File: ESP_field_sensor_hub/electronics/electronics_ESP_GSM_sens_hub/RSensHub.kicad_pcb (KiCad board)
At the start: 2 copper layers, 117 x 107 mm, 48 parts, among them J1 RJ45_Shielded, J2 RJ45_Shielded, J3 Conn_01x12_Male, J4 Conn_01x04_Female, Q4 IRF540N, U1 MAX48_module, U10 PC817, U11 PC817, U12 PC817, U2 5V5ADCDC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

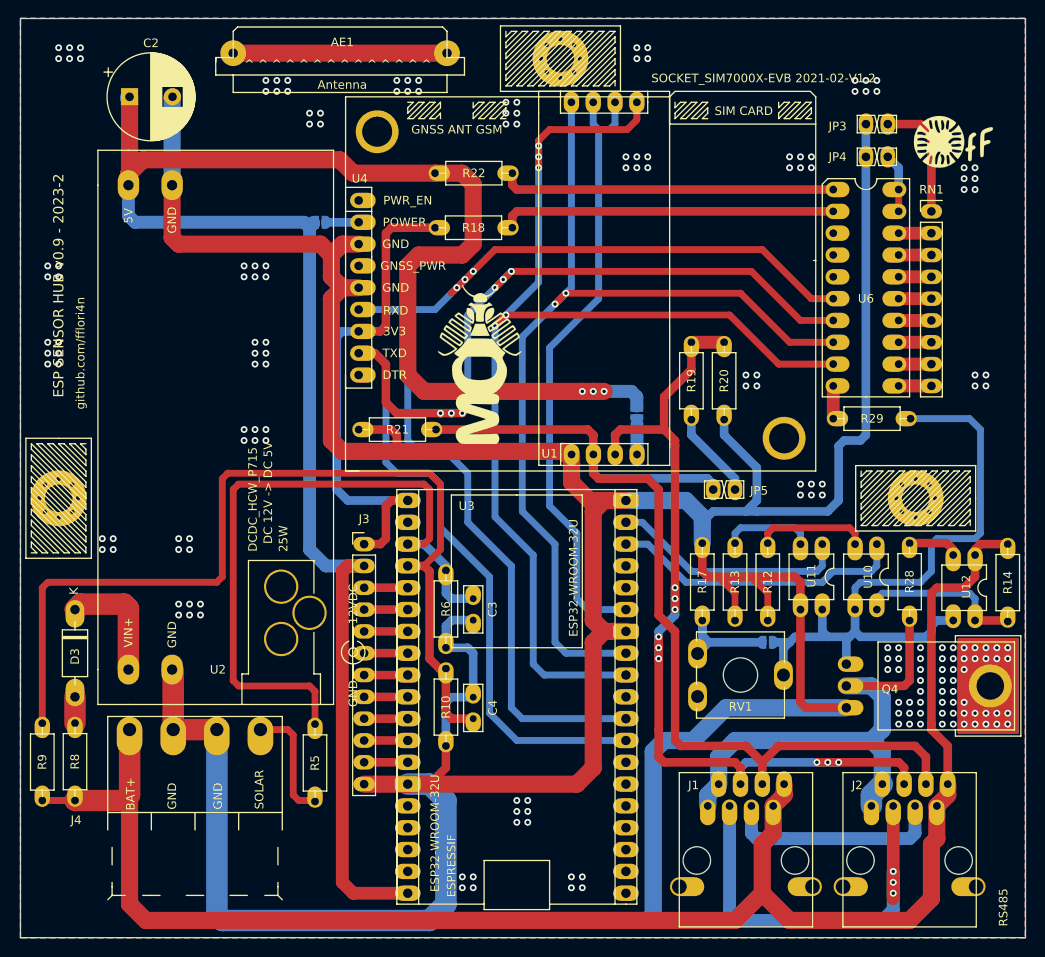
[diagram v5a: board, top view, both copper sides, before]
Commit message: started working on GNSS time and NTP functionality, ESP32 timekeeping works, just need to update it from modem. need to parse the GNSS status for string. Played around with chatGPT, and got a fairly good solution for converting datetimeString to unix time. @TODO: the SIM7000 class makes little sense, needs a refactoring. I have functions for geting CSQ and GNSS data from modem in a totally different class.
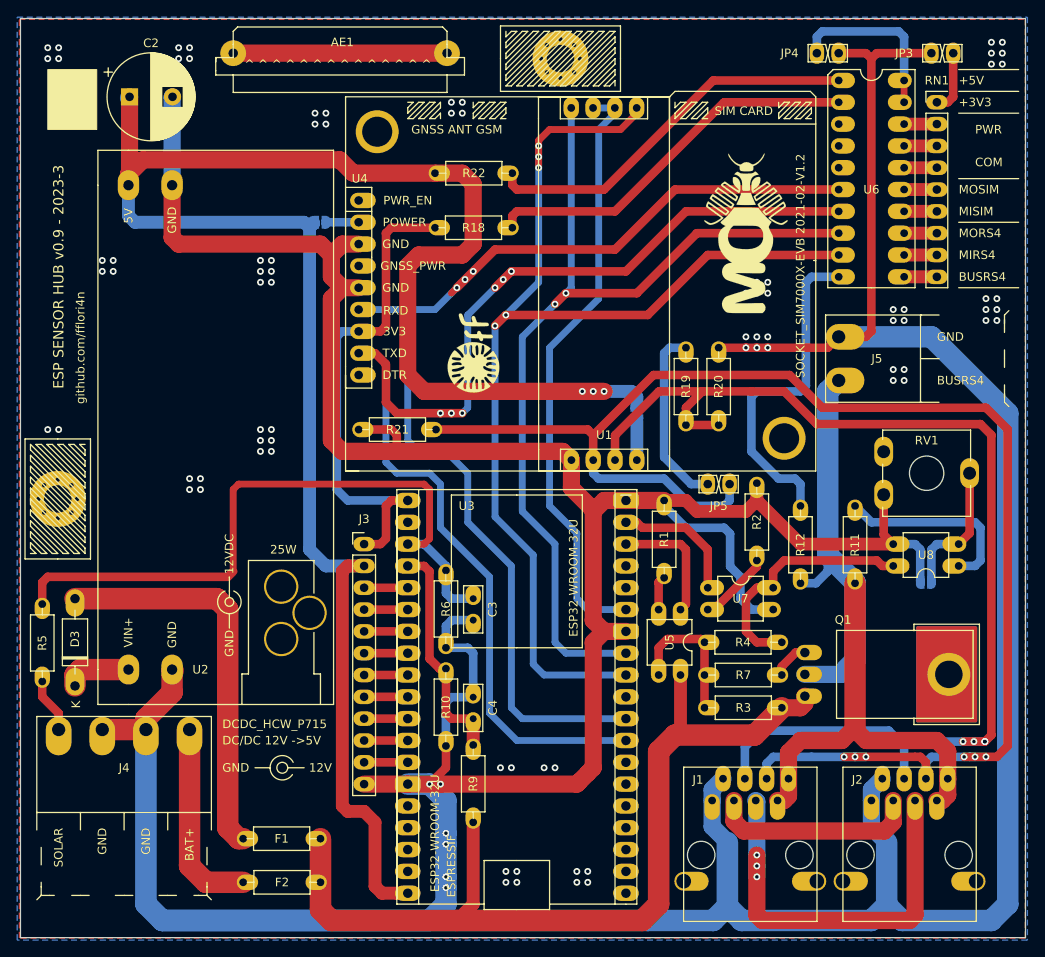
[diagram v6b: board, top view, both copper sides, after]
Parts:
- removed the G*** at (353.8, 62.2)
- removed the G*** at (358.4, 115.8)
- removed the G*** at (408.9, 36.3)
- removed Q4: IRF540N, myComponents:TO-220-3_Horizontal_TabDown_bothSides
- removed R13: 330R, myComponents:resistor0.25,9mm
- removed R14, R28, R29: 1K, myComponents:resistor0.25,9mm
- removed R17: 100K, myComponents:resistor0.25,9mm
- removed the REF** at (304.8, 77.9)
- removed the REF** at (404.6, 77.9)
- removed U10, U11, U12: PC817, myComponents:optoCouplerDIP4
- added F2: 0R, myComponents:resistor0.25,9mm, F.Cu at (335.3, 122.6)
- added G***: LOGO, myComponents:ma_Logo, B.Cu at (382.3, 38.7)
- added G***: LOGO, myComponents:xffLogo, B.Cu at (361.9, 115.6)
- added G***: LOGO, myComponents:xffLogo, F.Cu at (353.1, 61.0)
- added G***: LOGO, myComponents:ma_Logo, F.Cu at (384.8, 47.0)
- added J5: Conn_01x02_Male, myComponents:TerminalBlockRemovablex2, F.Cu at (395.6, 64.1)
- added Q1: IRF9540, myComponents:TO-220-3_Horizontal_TabDown_bothSides, F.Cu at (391.7, 95.8)
- added R1: 330R, myComponents:resistor0.25,9mm, F.Cu at (375.3, 87.1)
- added R11: 1K, myComponents:resistor0.25,9mm, F.Cu at (397.5, 87.7)
- added R2: 330R, myComponents:resistor0.25,9mm, F.Cu at (386.1, 85.1)
- added R3: 1K, myComponents:resistor0.25,9mm, F.Cu at (389.0, 102.2)
- added R4: 1K, myComponents:resistor0.25,9mm, F.Cu at (380.0, 94.6)
- added R7: 100, myComponents:resistor0.25,9mm, F.Cu at (389.0, 98.4)
- added REF**: M3 mechanical, myComponents:M3 mechanical, F.Cu at (304.7, 77.9)
- added U5: PC817, myComponents:optoCouplerDIP4, F.Cu at (377.2, 90.8)
- added U7: PC817, myComponents:optoCouplerDIP4, F.Cu at (380.4, 88.3)
- added U8: PC817, myComponents:optoCouplerDIP4, F.Cu at (409.6, 85.7)
- F1: renamed from R8; value R0 -> 0R
- R10, R6: value 2M -> 1K
- R12: value 330R -> 1K
- R5, R9: value 20M -> 10K
- RV1: value R_POT -> 10K
- moved R9 50.2 mm to (353.1, 115.6)
- moved R5 34.7 mm to (302.9, 99.2)
- moved RV1 32.0 mm to (400.8, 77.4)
- moved F1 23.7 mm to (326.3, 117.5), turned to 0 degrees
- moved JP6 19.7 mm to (405.8, 87.6)
- moved RN1 12.7 mm to (407.0, 31.8)
- moved U6 12.7 mm to (395.6, 29.2)
- moved JP4 12.5 mm to (395.6, 26.0), turned to 270 degrees
- moved JP3 11.2 mm to (406.4, 26.0)
- moved R19 9.66 mm to (377.8, 69.3), turned to 90 degrees
- moved R20 9.66 mm to (381.6, 69.3), turned to 90 degrees
- moved D3 8.89 mm to (306.7, 99.7), turned to 90 degrees
- moved J4 8.25 mm to (304.8, 104.8)
- moved R12 5.77 mm to (391.2, 87.7)
- moved JP5 3.24 mm to (380.4, 76.2), turned to 90 degrees
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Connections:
- net Net-(U3-Pad2) renamed /EN
- J1 pad 1: /SAFE_BAT_GND -> GND
- J1 pad 2: /SAFE_BAT_GND -> GND
- J1 pad 7: +BATT -> /SAFE_BAT+
- J1 pad 8: +BATT -> /SAFE_BAT+
- J2 pad 1: /SAFE_BAT_GND -> GND
- J2 pad 2: /SAFE_BAT_GND -> GND
- J2 pad 7: +BATT -> /SAFE_BAT+
- J2 pad 8: +BATT -> /SAFE_BAT+
- J4 pad 1: +BATT -> /V_SOLAR
- J4 pad 4: /V_SOLAR -> Net-(FUSE2-Pad2)
- JP6 pad 1: Net-(JP6-Pad1) -> GND
- R12 pad 1: GND -> /SAFE_BAT+
- R12 pad 2: Net-(R12-Pad2) -> /VBUS_LED
- RV1 pad 1: Net-(RV1-Pad1) -> GND
- RV1 pad 3: Net-(JP6-Pad1) -> Net-(RV1-Pad3)
- U3 pad 21: /Vout_OFF -> /Vout_ON
- U3 pad 22: /Vout_ON -> /Vout_OFF
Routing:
- net GND: track 489.0 -> 661.3 mm, vias 126 -> 88
- net /SAFE_BAT+: track 0.00 -> 97.6 mm
- net +BATT: track 200.2 -> 106.4 mm
- net /VN_PIN: track 109.2 -> 27.0 mm
- net Net-(JP6-Pad2): track 78.7 -> 16.0 mm
- net /RS485_A: track 115.2 -> 177.3 mm, vias 0 -> 6
- net /SAFE_BAT_GND: track 58.4 -> 0.00 mm
- net Net-(D3-Pad2): track 3.06 -> 46.0 mm
- net /VBUS_LED: track 3.81 -> 39.2 mm
- net /RS485_B: track 106.4 -> 136.6 mm, vias 9 -> 4
- net Net-(R4-Pad2): track 0.00 -> 28.9 mm
- net /BUS_3: track 47.4 -> 24.4 mm, vias 3 -> 0
- net Net-(FUSE2-Pad2): track 0.00 -> 22.9 mm
- net /BUS_5: track 25.9 -> 48.2 mm, vias 0 -> 3
- net Net-(R11-Pad2): track 0.00 -> 22.3 mm
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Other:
- board text added: "+3V3"
- board text added: "+5V"
- board text added: "12V"
- board text added: "BUSRS4"
- board text added: "COM"
- board text added: "ESP SENSOR HUB v0.9 - 2023-3"
- board text added: "MIRS4"
- board text added: "MISIM"
- board text added: "MORS4"
- board text added: "MOSIM"
- board text added: "PWR"
- board text removed: "ESP SENSOR HUB v0.9 - 2023-2"
- board text removed: "RS485"
